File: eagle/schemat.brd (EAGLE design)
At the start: 27 parts, among them IC1 MEGA8-AI, Q1 N-MOSFET BSS138, Q2 N-MOSFET BSS138, U1 LCD-16X2SILK, X2 MINI-USB-32005-301, Y1 16MHz

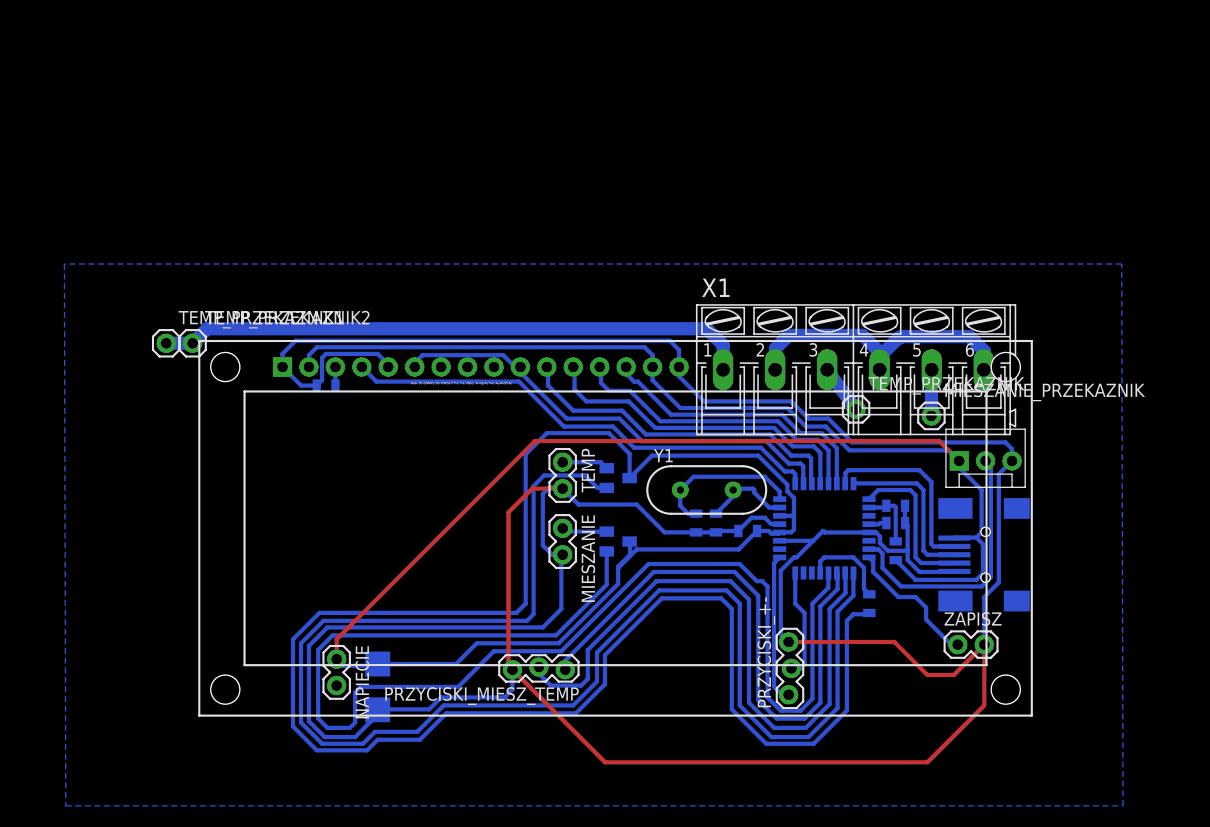
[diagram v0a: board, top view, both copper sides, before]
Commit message: Poprawiony schemat
Nie dało się przylutować microUSB (zła biblioteka)
Nie podłączony RESET
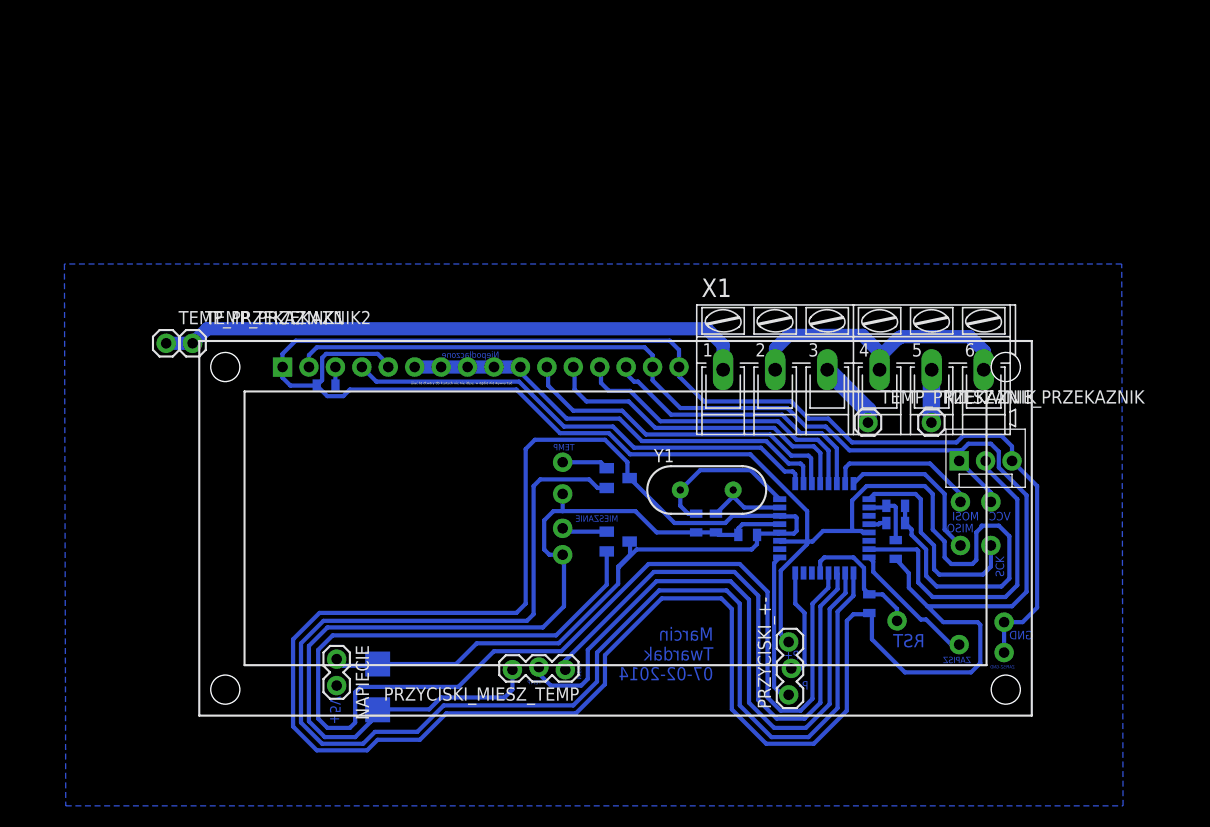
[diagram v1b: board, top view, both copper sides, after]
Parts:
- removed X2: MINI-USB-32005-301, con-cypressindustries:32005-301
- added GND, MIESZANIE_GND, MISO, MOSI, RESET, SCK, TEMP_GND, VCC, ZAPISZ_GND: M01NOSILK-KIT, SparkFun-Connectors:1X01NS-KIT
- MIESZANIE, TEMP, ZAPISZ: value M02PTH -> M01NOSILK-KIT; device SparkFun-Connectors:1X02 -> SparkFun-Connectors:1X01NS-KIT
- moved TEMP_PRZEKAZNIK 1.71 mm to (70.0, 90.2)
- moved MIESZANIE_PRZEKAZNIK 0.64 mm to (76.1, 90.2)
- moved C5 0.38 mm to (58.4, 79.4)
- moved L1 0.13 mm to (72.6, 78.0)
- moved ZAPISZ 0.13 mm to (78.7, 68.8)
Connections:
- removed net N$1: IC1.29, R1.1
- new net RESET: IC1.29, R1.1, RESET.1
- net +5V: now also VCC.1; no longer X2.1
- net GND: now also GND.1, MIESZANIE_GND.1, TEMP_GND.1, ZAPISZ_GND.1; no longer MIESZANIE.2, TEMP.2, X2.5, ZAPISZ.2
- net MISO: now also MISO.1; no longer X2.3
- net MOSI: now also MOSI.1; no longer X2.2
- net SCK: now also SCK.1; no longer X2.4
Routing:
- net +5V: track 387.2 -> 354.1 mm
- net RESET: track 0.00 -> 13.0 mm
- net N$1: track 8.63 -> 0.00 mm
- net GND: track 343.9 -> 335.5 mm
- net LM35: track 25.8 -> 31.6 mm
- net SCK: track 15.0 -> 20.7 mm
- net MOSI: track 18.2 -> 14.7 mm
- net N$13: track 4.74 -> 6.74 mm
- net E: track 44.1 -> 43.3 mm
- net MISO: track 16.2 -> 15.5 mm
- net N$14: track 4.46 -> 5.09 mm
- net ZAPISZ: track 13.3 -> 12.7 mm
- net N$7: track 8.38 -> 7.87 mm
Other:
- board text added: "+5V"
- board text added: "GND"
- board text added: "MIESZ"
- board text added: "MIESZANIE"
- board text added: "MISO"
- board text added: "MOSI"
- board text added: "Marcin Twardak 07-02-2014"
- board text added: "Niepodłączone"
- board text added: "P+"
- board text added: "P-"
- board text added: "RST"
- board text added: "SCK"
- board text added: "TEMP"
- board text added: "VCC"
- board text added: "ZAPISZ"
- board text added: "ZAPISZ-GND"

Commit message: uzupełniony opis schematu
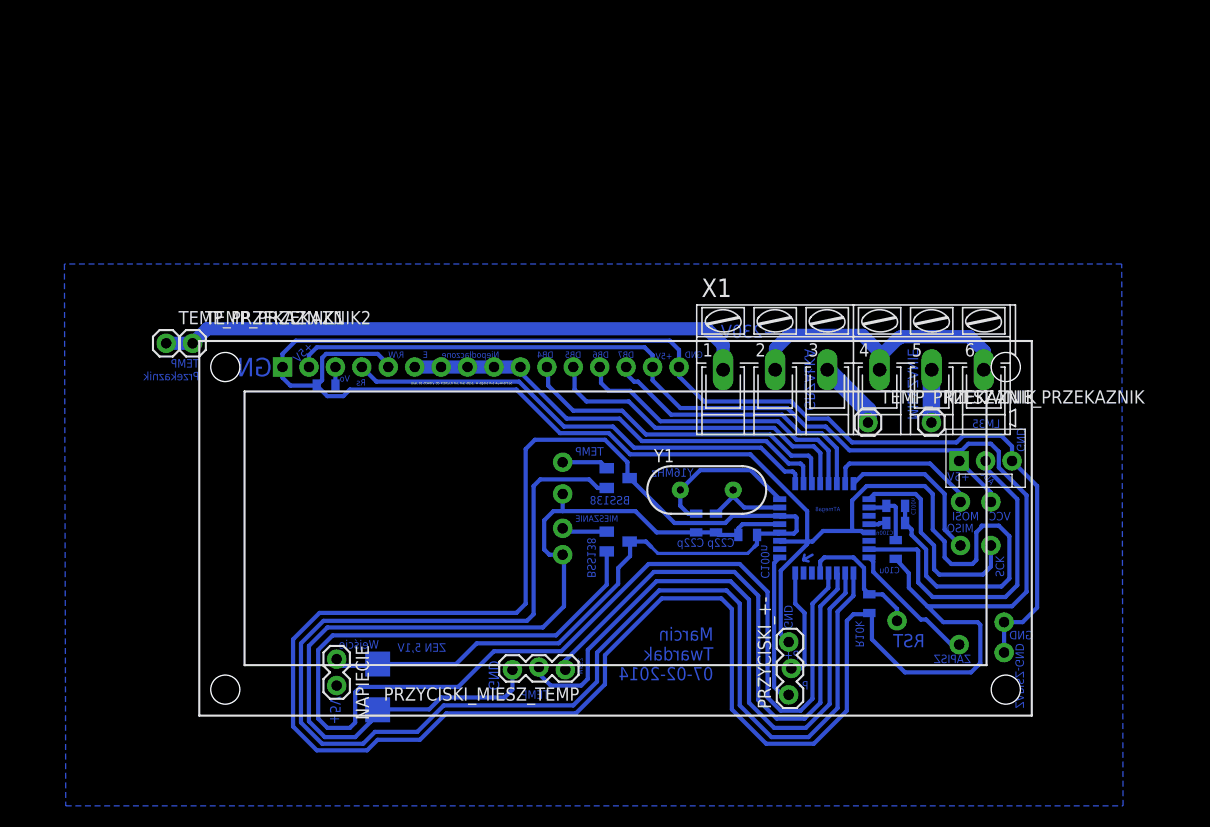
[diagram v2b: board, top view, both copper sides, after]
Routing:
- net N$1: track 0.00 -> 2.07 mm
- net +5V: track 354.1 -> 352.9 mm
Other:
- board text added: "ADC"
- board text added: "ATmega8"
- board text added: "BSS138"
- board text added: "C100n"
- board text added: "C10u"
- board text added: "C22p"
- board text added: "DB4"
- board text added: "DB5"
- board text added: "DB6"
- board text added: "DB7"
- board text added: "E"
- board text added: "GRZAŁKA"
- board text added: "LM35"
- board text added: "R/W"
- board text added: "R10k"
- board text added: "Rs"
- board text added: "TEMP Przekaznik"
- board text added: "Vo"
- board text added: "Wejście"
- board text added: "Y16MHz"
- board text added: "ZEN 5,1V"
- board text added: "~230V"

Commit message: Dodane opisy + wersja do druku
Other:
- board text added: "ATmega8/88"
- board text added: "Sterownik do wytrawiarki"
- board text added: "https://github.com/twardakm/"
- board text removed: "ATmega8"
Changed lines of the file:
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@@
 <text x="43.815" y="79.121" size="0.8128" layer="16" rot="MR270">BSS138</text>
 <text x="24.765" y="68.961" size="0.8128" layer="16" rot="MR180">ZEN 5,1V</text>
-<text x="82.677" y="89.662" size="0.8128" layer="16" rot="MR0">LM35</text>
+<text x="82.677" y="89.662" size="1.016" layer="16" rot="MR0">LM35</text>
 <text x="79.756" y="84.582" size="0.8128" layer="16" rot="MR0">+5V</text>
 <text x="81.788" y="84.126603125" size="0.6096" layer="16" rot="MR45">ADC</text>
-<text x="85.09" y="89.662" size="0.8128" layer="16" rot="MR270">GND</text>
+<text x="85.471" y="90.551" size="1.016" layer="16" rot="MR270">GND</text>
 <text x="69.596" y="71.12" size="0.8128" layer="16" rot="MR270">R10k</text>
 <text x="73.025" y="75.692" size="0.6096" layer="16" rot="MR0">C10u</text>
 <text x="72.39" y="79.375" size="0.4064" layer="16" rot="MR0">C100n</text>
 <text x="74.549" y="82.931" size="0.4064" layer="16" rot="MR270">C100n</text>
-<text x="67.31" y="81.661" size="0.4064" layer="16" rot="MR0">ATmega8</text>
+<text x="67.183" y="82.677" size="0.4064" layer="16" rot="MR0">ATmega8/88</text>
 <text x="59.69" y="75.184" size="0.8128" layer="16" rot="MR90">C100n</text>
 <text x="54.229" y="78.232" size="0.8128" layer="16" rot="MR0">C22p</text>
@@
 <text x="34.544" y="67.31" size="1.016" layer="16" rot="MR270">GND</text>
 <text x="62.738" y="72.644" size="0.8128" layer="16" rot="MR270">GND</text>
+<text x="56.134" y="64.262" size="0.6096" layer="16" rot="MR0">https://github.com/twardakm/</text>
+<text x="56.261" y="62.865" size="0.8128" layer="16" rot="MR0">Sterownik do wytrawiarki</text>
 </plain>
 <attributes>

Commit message: kolejne poprawki
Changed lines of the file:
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@@
 <contactref element="IC1" pad="23"/>
 <contactref element="LM35" pad="2"/>
-<wire x1="74.803" y1="77.851" x2="74.676" y2="77.978" width="0.4064" layer="16"/>
-<wire x1="74.676" y1="77.978" x2="70.1106" y2="77.978" width="0.4064" layer="16"/>
 <wire x1="70.1106" y1="77.978" x2="70.0786" y2="78.01" width="0.4064" layer="16"/>
 <wire x1="84.328" y1="74.549" x2="83.185" y2="73.406" width="0.4064" layer="16"/>
 <wire x1="83.185" y1="73.406" x2="76.2" y2="73.406" width="0.4064" layer="16"/>
 <wire x1="76.2" y1="73.406" x2="74.803" y2="74.803" width="0.4064" layer="16"/>
-<wire x1="74.803" y1="74.803" x2="74.803" y2="77.851" width="0.4064" layer="16"/>
 <wire x1="84.328" y1="74.549" x2="84.328" y2="82.804" width="0.4064" layer="16"/>
 <wire x1="84.328" y1="82.804" x2="81.28" y2="85.852" width="0.4064" layer="16"/>
 <wire x1="81.28" y1="85.852" x2="81.28" y2="86.487" width="0.4064" layer="16"/>
+<wire x1="70.1106" y1="77.978" x2="74.041" y2="77.978" width="0.4064" layer="16"/>
+<wire x1="74.041" y1="77.978" x2="74.422" y2="77.597" width="0.4064" layer="16"/>
+<wire x1="74.422" y1="77.597" x2="74.422" y2="76.835" width="0.4064" layer="16"/>
+<wire x1="74.422" y1="76.835" x2="74.803" y2="76.454" width="0.4064" layer="16"/>
+<wire x1="74.803" y1="76.454" x2="74.803" y2="74.803" width="0.4064" layer="16"/>
 </signal>
 <signal name="TEMP">

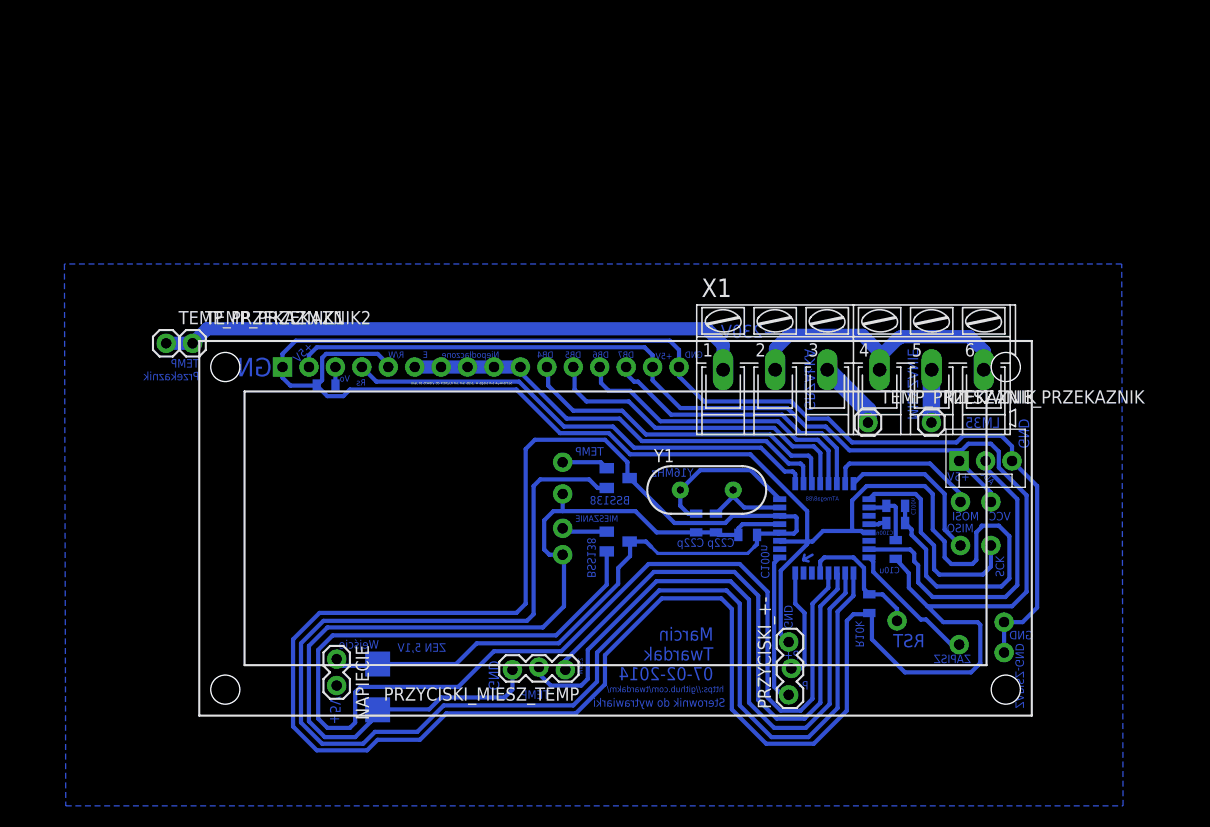
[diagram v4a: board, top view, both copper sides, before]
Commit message: Zmieniony schemat + zmiany w programie
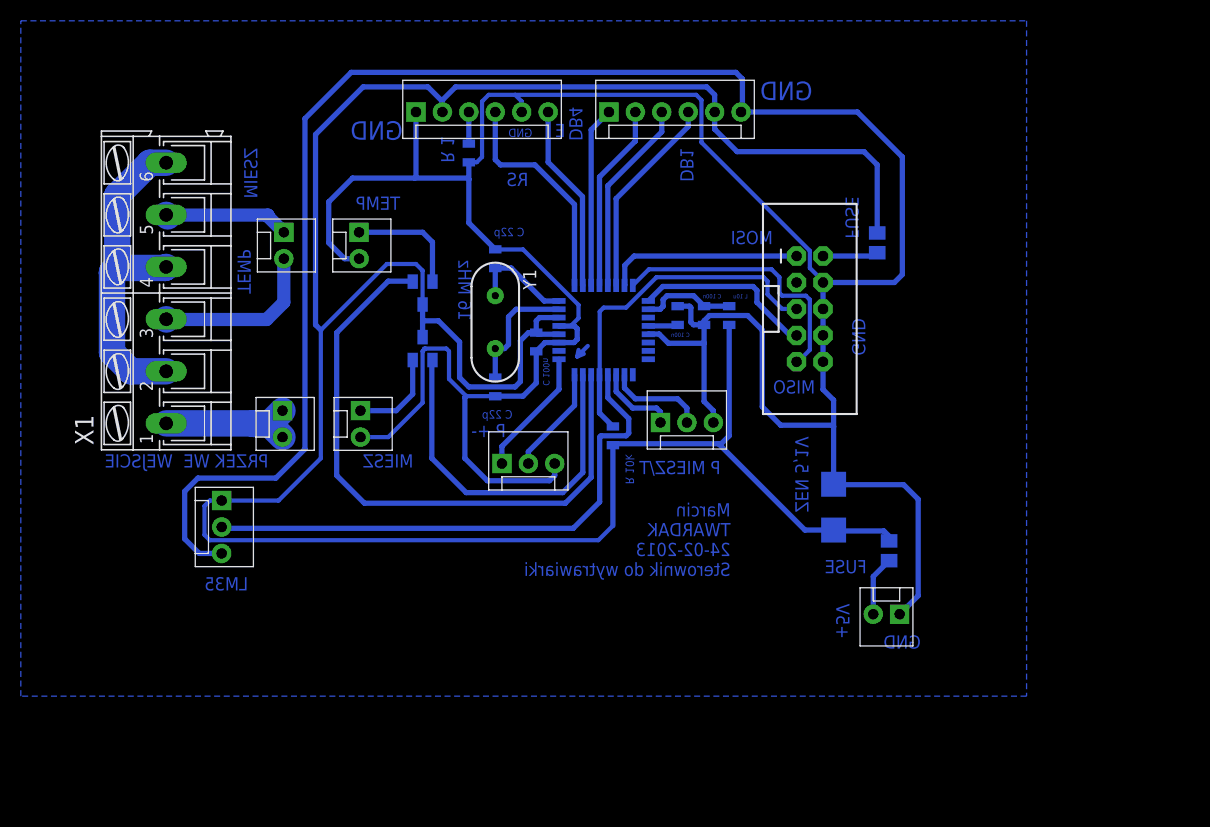
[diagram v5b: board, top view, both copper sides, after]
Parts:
- removed GND, MIESZANIE_GND, MISO, MOSI, RESET, SCK, TEMP_GND, VCC, ZAPISZ, ZAPISZ_GND: M01NOSILK-KIT, SparkFun-Connectors:1X01NS-KIT
- removed MIESZANIE_PRZEKAZNIK, TEMP_PRZEKAZNIK1, TEMP_PRZEKAZNIK2: M01PTH, SparkFun-Connectors:1X01
- removed R2: 1, SparkFun-Passives:0805
- removed U1: LCD-16X2SILK, SparkFun-Displays:LCD-16X2
- added LCD1, LCD2: (no value), SparkFun-Connectors:MOLEX-1X6
- added PRZEKAZNIK_NAPIECIE: M02POLAR, SparkFun-Connectors:MOLEX-1X2
- added R3, R4: FUSE 500mA, resistor:M0805
- added R5: 1, SparkFun-Passives:0805
- added U$2: AVR_SPI_PROG2PTH2, SparkFun-Connectors:2X5-SHROUDED
- MIESZANIE, TEMP: value M01NOSILK-KIT -> M02POLAR; device SparkFun-Connectors:1X01NS-KIT -> SparkFun-Connectors:MOLEX-1X2
- NAPIECIE: value M02PTH -> M02POLAR; device SparkFun-Connectors:1X02 -> SparkFun-Connectors:MOLEX-1X2
- PRZYCISKI_+-, PRZYCISKI_MIESZ_TEMP: device SparkFun-Connectors:1X03_LOCK -> SparkFun-Connectors:MOLEX-1X3
- TEMP_PRZEKAZNIK: value M01PTH -> M02POLAR; device SparkFun-Connectors:1X01 -> SparkFun-Connectors:MOLEX-1X2
- moved LM35 71.0 mm to (7.87, 82.7), turned to 270 degrees
- moved X1 66.4 mm to (2.54, 102.6), turned to 90 degrees
- moved TEMP_PRZEKAZNIK 59.0 mm to (13.8, 108.5), turned to 270 degrees
- moved NAPIECIE 54.3 mm to (73.0, 71.8), turned to 180 degrees
- moved U$1 47.1 mm to (66.7, 82.0), turned to 90 degrees
- moved PRZYCISKI_+- 35.5 mm to (34.8, 86.2), turned to 0 degrees
- moved C4 31.9 mm to (34.2, 105.9), turned to 270 degrees
- moved TEMP 29.5 mm to (21.1, 108.5)
- moved R1 29.4 mm to (45.5, 88.9)
- moved C1 28.9 mm to (51.7, 100.5), turned to 270 degrees
- moved IC1 28.5 mm to (44.6, 99.1)
- moved L1 27.6 mm to (56.6, 100.5)
- moved C5 27.5 mm to (38.1, 97.9), turned to 90 degrees
- moved Q2 26.4 mm to (27.2, 97.3), turned to 0 degrees
- moved C2 26.0 mm to (54.2, 100.5), turned to 90 degrees
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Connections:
- removed net N$13: TEMP_PRZEKAZNIK.1, X1.3
- removed net N$9: R2.1, U1.3
- removed net VCC: NAPIECIE.2
- new net N$10: TEMP_PRZEKAZNIK.2, X1.3
- new net N$11: R4.1, U$2.2
- new net N$16: LCD2.3, R5.1
- new net N$8: NAPIECIE.2, R3.1
- net +5V: now also LCD1.5, LCD2.2, R3.2, R4.2; no longer NAPIECIE.1, U1.15, U1.2, VCC.1
- net DB4: now also LCD1.1; no longer U1.11
- net DB5: now also LCD1.2; no longer U1.12
- net DB6: now also LCD1.3; no longer U1.13
- net DB7: now also LCD1.4; no longer U1.14
- net E: now also LCD2.6; no longer U1.6
- net GND: now also LCD1.6, LCD2.1, LCD2.5, MIESZANIE.2, NAPIECIE.1, R5.2, TEMP.2, U$2.10, U$2.4, U$2.6, U$2.8; no longer GND.1, MIESZANIE_GND.1, R2.2, TEMP_GND.1, U1.1, U1.16, U1.5, ZAPISZ_GND.1
- net LM35: now also IC1.28; no longer IC1.23
- net MIESZANIE: now also IC1.31; no longer IC1.28
- net MISO: now also U$2.9; no longer MISO.1
- net MOSI: now also U$2.1; no longer MOSI.1
- net N$14: now also TEMP_PRZEKAZNIK.1; no longer MIESZANIE_PRZEKAZNIK.1
- net RESET: now also U$2.5; no longer RESET.1
- net RS: now also LCD2.4; no longer U1.4
- net SCK: now also U$2.7; no longer SCK.1
- net TEMP: now also IC1.30; no longer IC1.25
- net VDD: now also PRZEKAZNIK_NAPIECIE.1, PRZEKAZNIK_NAPIECIE.2; no longer TEMP_PRZEKAZNIK1.1, TEMP_PRZEKAZNIK2.1
- net ZAPISZ: no longer ZAPISZ.1
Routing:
- net +5V: track 352.9 -> 253.2 mm
- net MIESZANIE: track 121.2 -> 35.5 mm
- net TEMP: track 137.6 -> 59.5 mm
- net PRZYCISK_TEMP: track 60.7 -> 9.46 mm
- net PRZYCISK_MIESZANIE: track 54.5 -> 7.70 mm
- net VDD: track 57.1 -> 13.5 mm
- net GND: track 335.5 -> 378.6 mm
- net E: track 43.3 -> 18.1 mm
- net RS: track 46.8 -> 21.8 mm
- net LM35: track 31.2 -> 53.0 mm
- net RESET: track 13.0 -> 33.9 mm
- net N$10: track 0.00 -> 16.2 mm
- net DB4: track 32.5 -> 17.4 mm
- net DB5: track 31.3 -> 18.1 mm
- net ZAPISZ: track 12.7 -> 0.00 mm
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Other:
- board text added: "16 MHz"
- board text added: "C 100n"
- board text added: "C 22p"
- board text added: "DB1"
- board text added: "FUSE"
- board text added: "L 10u"
- board text added: "Marcin TWARDAK 24-02-2013 Sterownik do wytrawiarki"
- board text added: "P +-"
- board text added: "P MIESZ/T"
- board text added: "PRZEK WE"
- board text added: "R 1"
- board text added: "R 10k"
- board text added: "RS"
- board text added: "WEJSCIE"
- board text removed: "ADC"
- board text removed: "ATmega8/88"
- board text removed: "BSS138"
- board text removed: "C100n"
- board text removed: "C10u"
- board text removed: "C22p"
- board text removed: "DB5"
- board text removed: "DB6"
- board text removed: "DB7"
- board text removed: "GRZAŁKA"
- board text removed: "MIESZANIE"
- board text removed: "Marcin Twardak 07-02-2014"
- board text removed: "Niepodłączone"
- board text removed: "Olać te otwory do ktorych nic nie idzie, w ogóle nie wywiercać"
- board text removed: "P+"
- board text removed: "P-"
- board text removed: "R/W"
- board text removed: "R10k"
- board text removed: "RST"
- board text removed: "Rs"
- board text removed: "SCK"
- board text removed: "Sterownik do wytrawiarki"
- board text removed: "TEMP Przekaznik"
- board text removed: "VCC"
- board text removed: "Vo"
- board text removed: "Wejście"
- board text removed: "Y16MHz"
- board text removed: "ZAPISZ"
- board text removed: "ZAPISZ-GND"
- board text removed: "https://github.com/twardakm/"
- board text removed: "~230V"
